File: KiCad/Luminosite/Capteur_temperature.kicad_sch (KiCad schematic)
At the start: 17 parts, among them J2 Conn_01x03, Q1 BC547, Q2 BC547, U2 MCP6022, U3 TL431D

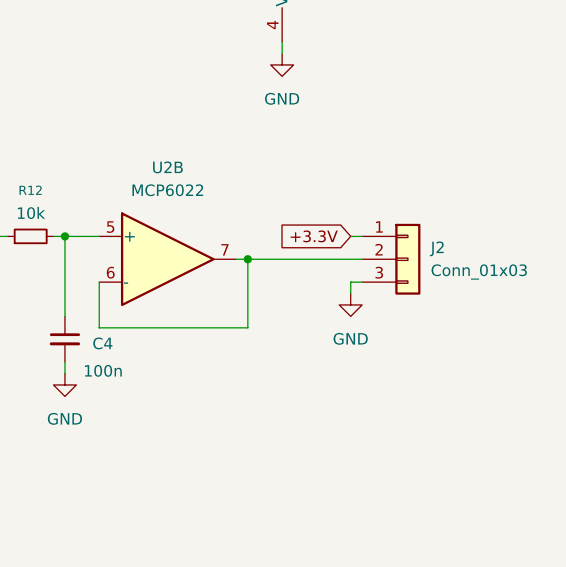
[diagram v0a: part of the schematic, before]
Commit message: Ajout des empreintes pour le PCB
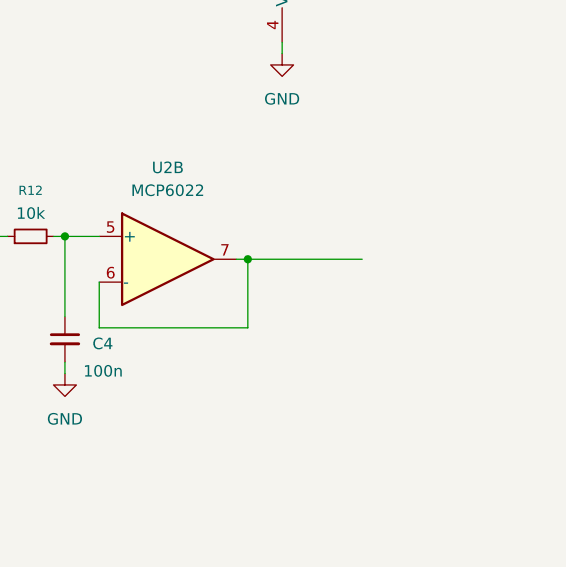
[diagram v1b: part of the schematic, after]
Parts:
- removed J2: Conn_01x03, symbol Connector_Generic:Conn_01x03
- C4, C5: footprint (none) -> Capacitor_SMD:C_0201_0603Metric_Pad0.64x0.40mm_HandSolder
- R10, R11, R12, R13, R14, R15, R7, R8, R9: footprint (none) -> Resistor_SMD:R_0201_0603Metric_Pad0.64x0.40mm_HandSolder
- U2: footprint (none) -> MCP6022:SOP8P65_300X640X120L60X24N
